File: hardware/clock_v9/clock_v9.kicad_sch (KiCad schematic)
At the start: 189 parts, among them J1 RJ45, J14 DC-063-25A, J2 Conn_01x03, J4 USB_C_Receptacle, J5 Conn_01x06_Pin, J8 Conn_01x02, Q1 2N7002, Q10 2N7002, Q2 S8550, Q3 S8050, Q4 S8050, Q5 S8050, Q9 2N7002, SW1 LC1258OASP, U1 ADA4807-1, U10 STM32F405RGTx, U11 AMS1117-3.3, U12 BA50DD0WHFP-TR, U13 M24C02-RMN, U14 CH340C, U15 USBLC6-2P6, U16 TLV3603DCKR, U17 SN74LVC1G14DBV, U18 TMP102xxDRL, U2 SN74LVC1G14DBV, U3 SN74LVC1G14DBV, U4 ADA4807-1, U5 ADA4807-1, U6 TLV3603DCKR, U7 SN74LVC1G14DBV, U8 TLV3603DCKR, U9 L78L05_SOT89, Y1 AOCJY4A-10.000MHZ-SW, Y2 16MHz

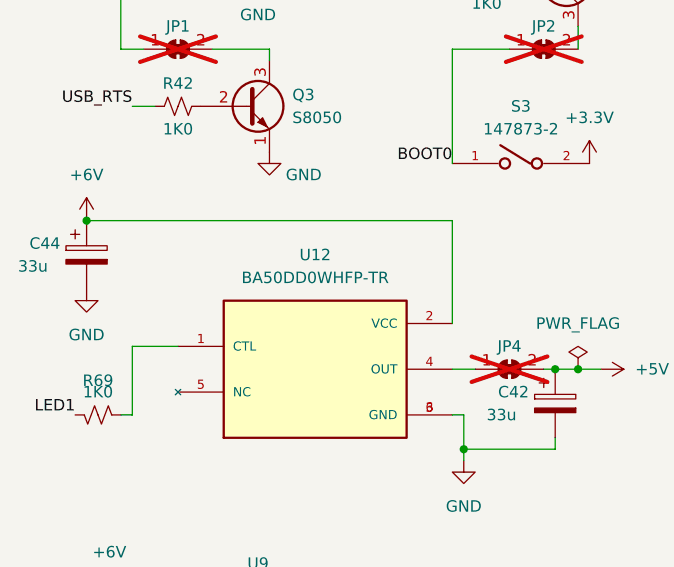
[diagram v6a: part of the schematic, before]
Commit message: start routing GPS RS232 inverts
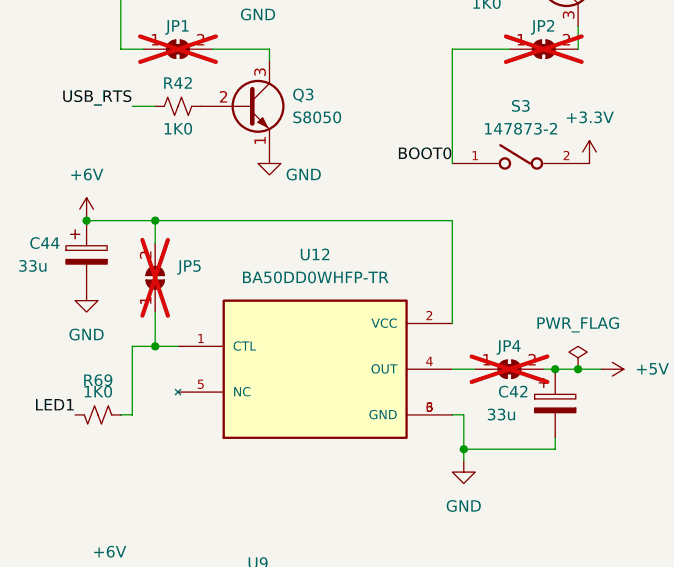
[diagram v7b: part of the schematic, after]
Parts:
- added JP5: SolderJumper_2_Open, Jumper:SolderJumper-2_P1.3mm_Open_RoundedPad1.0x1.5mm, symbol Jumper:SolderJumper_2_Open
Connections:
- net +6V: now also JP5.2 (B)
- net at R69.1, U12.1 (CTL): now also JP5.1 (A)
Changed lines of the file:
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@@
   (junction (at 273.05 88.9) (diameter 0) (color 0 0 0 0)
   )
+  (junction (at 29.21 154.94) (diameter 0) (color 0 0 0 0)
+  )
   (junction (at 387.35 25.4) (diameter 0) (color 0 0 0 0)
   )
@@
   (junction (at 269.24 251.46) (diameter 0) (color 0 0 0 0)
   )
+  (junction (at 29.21 168.91) (diameter 0) (color 0 0 0 0)
+  )
   (junction (at 236.22 252.73) (diameter 0) (color 0 0 0 0)
   )
@@
     (stroke (width 0) (type default))
   )
+  (wire (pts (xy 29.21 154.94) (xy 62.23 154.94))
+    (stroke (width 0) (type default))
+  )
+  (wire (pts (xy 29.21 154.94) (xy 29.21 157.48))
+    (stroke (width 0) (type default))
+  )
   (wire (pts (xy 48.26 199.39) (xy 50.8 199.39))
     (stroke (width 0) (type default))
@@
     (stroke (width 0) (type default))
   )
-  (wire (pts (xy 26.67 168.91) (xy 31.75 168.91))
+  (wire (pts (xy 26.67 168.91) (xy 29.21 168.91))
     (stroke (width 0) (type default))
   )
@@
     (stroke (width 0) (type default))
   )
+  (wire (pts (xy 29.21 165.1) (xy 29.21 168.91))
+    (stroke (width 0) (type default))
+  )
   (wire (pts (xy 195.58 123.19) (xy 195.58 121.92))
     (stroke (width 0) (type default))
@@
     (stroke (width 0) (type default))
   )
-  (wire (pts (xy 21.59 154.94) (xy 62.23 154.94))
+  (wire (pts (xy 21.59 154.94) (xy 29.21 154.94))
     (stroke (width 0) (type default))
   )
@@
     (stroke (width 0) (type default))
   )
+  (wire (pts (xy 29.21 168.91) (xy 31.75 168.91))
+    (stroke (width 0) (type default))
+  )
   (wire (pts (xy 204.47 171.45) (xy 204.47 172.72))
     (stroke (width 0) (type default))
@@
         )
       )
+    )
+  )
+  (symbol (lib_id "Jumper:SolderJumper_2_Open") (at 29.21 161.29 90) (unit 1)
+    (in_bom no) (on_board yes) (dnp yes) (fields_autoplaced)
+    (property "Reference" "JP5" (at 31.75 160.02 90)
+      (effects (font (size 1.27 1.27)) (justify right))
+    )
+    (property "Value" "SolderJumper_2_Open" (at 31.75 162.56 90)
+      (effects (font (size 1.27 1.27)) (justify right) hide)
+    )
+    (property "Footprint" "Jumper:SolderJumper-2_P1.3mm_Open_RoundedPad1.0x1.5mm" (at 29.21 161.29 0)
+      (effects (font (size 1.27 1.27)) hide)
+    )
+    (property "Datasheet" "~" (at 29.21 161.29 0)
+      (effects (font (size 1.27 1.27)) hide)
+    )
+    (pin "1")
+    (pin "2")
+    (instances
+      (project "clock_v9"
+        (path "/bd4d3b9a-07c1-4a53-9c94-2893f3e869d4"
+          (reference "JP5") (unit 1)
+        )
+      )

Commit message: route new TX/RX
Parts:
- SW1: footprint Footprints:LC1258OASP -> blinky_footprints:LC1258OASP
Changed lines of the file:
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@@
       (effects (font (size 1.524 1.524)))
     )
-    (property "Footprint" "Footprints:LC1258OASP" (at 99.06 105.41 0)
+    (property "Footprint" "blinky_footprints:LC1258OASP" (at 99.06 105.41 0)
       (effects (font (size 1.27 1.27) italic) hide)
     )
